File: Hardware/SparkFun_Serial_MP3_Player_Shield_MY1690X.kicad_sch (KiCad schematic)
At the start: 34 parts, among them J1 3.5mm TRRS, J3 Conn_01x03, J4 USB_C_Receptacle, J6 microSD, Q1 BSS138, SW1 SMD_5.2x5.2mm_h2.5mm, U2 MY1690X

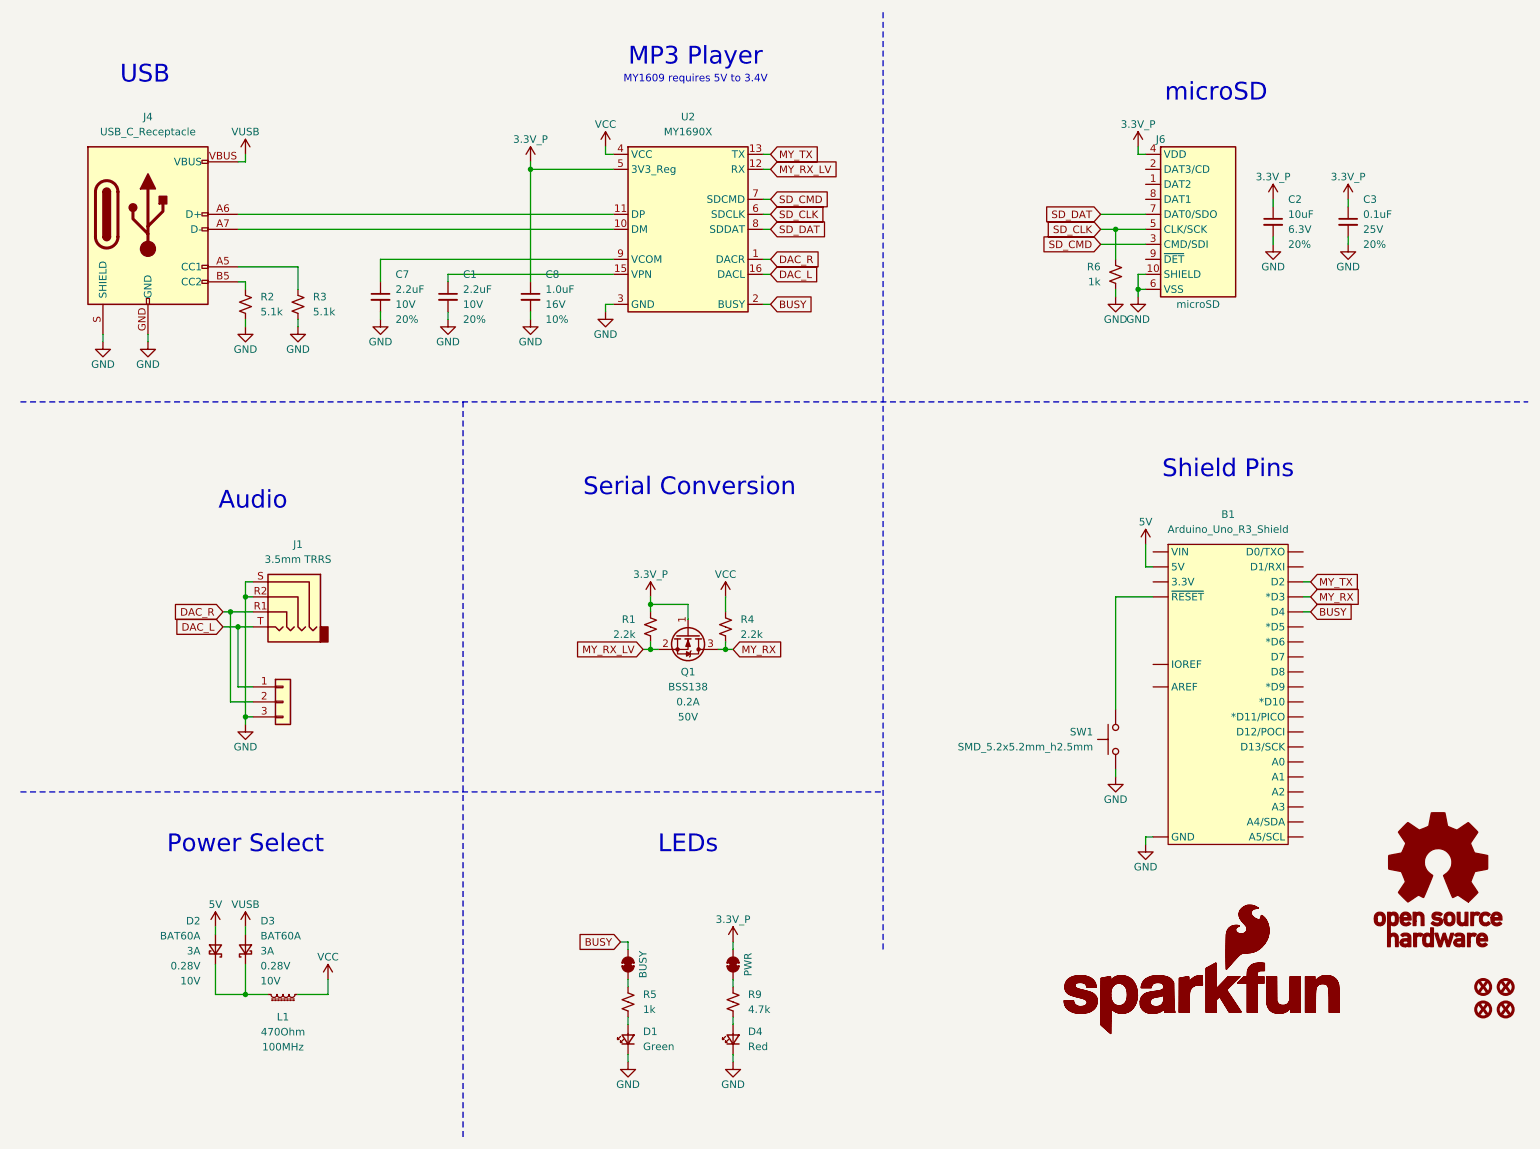
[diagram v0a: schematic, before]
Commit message: Add Busy LED, inline caps to TRRS, card detect, and power filtering.
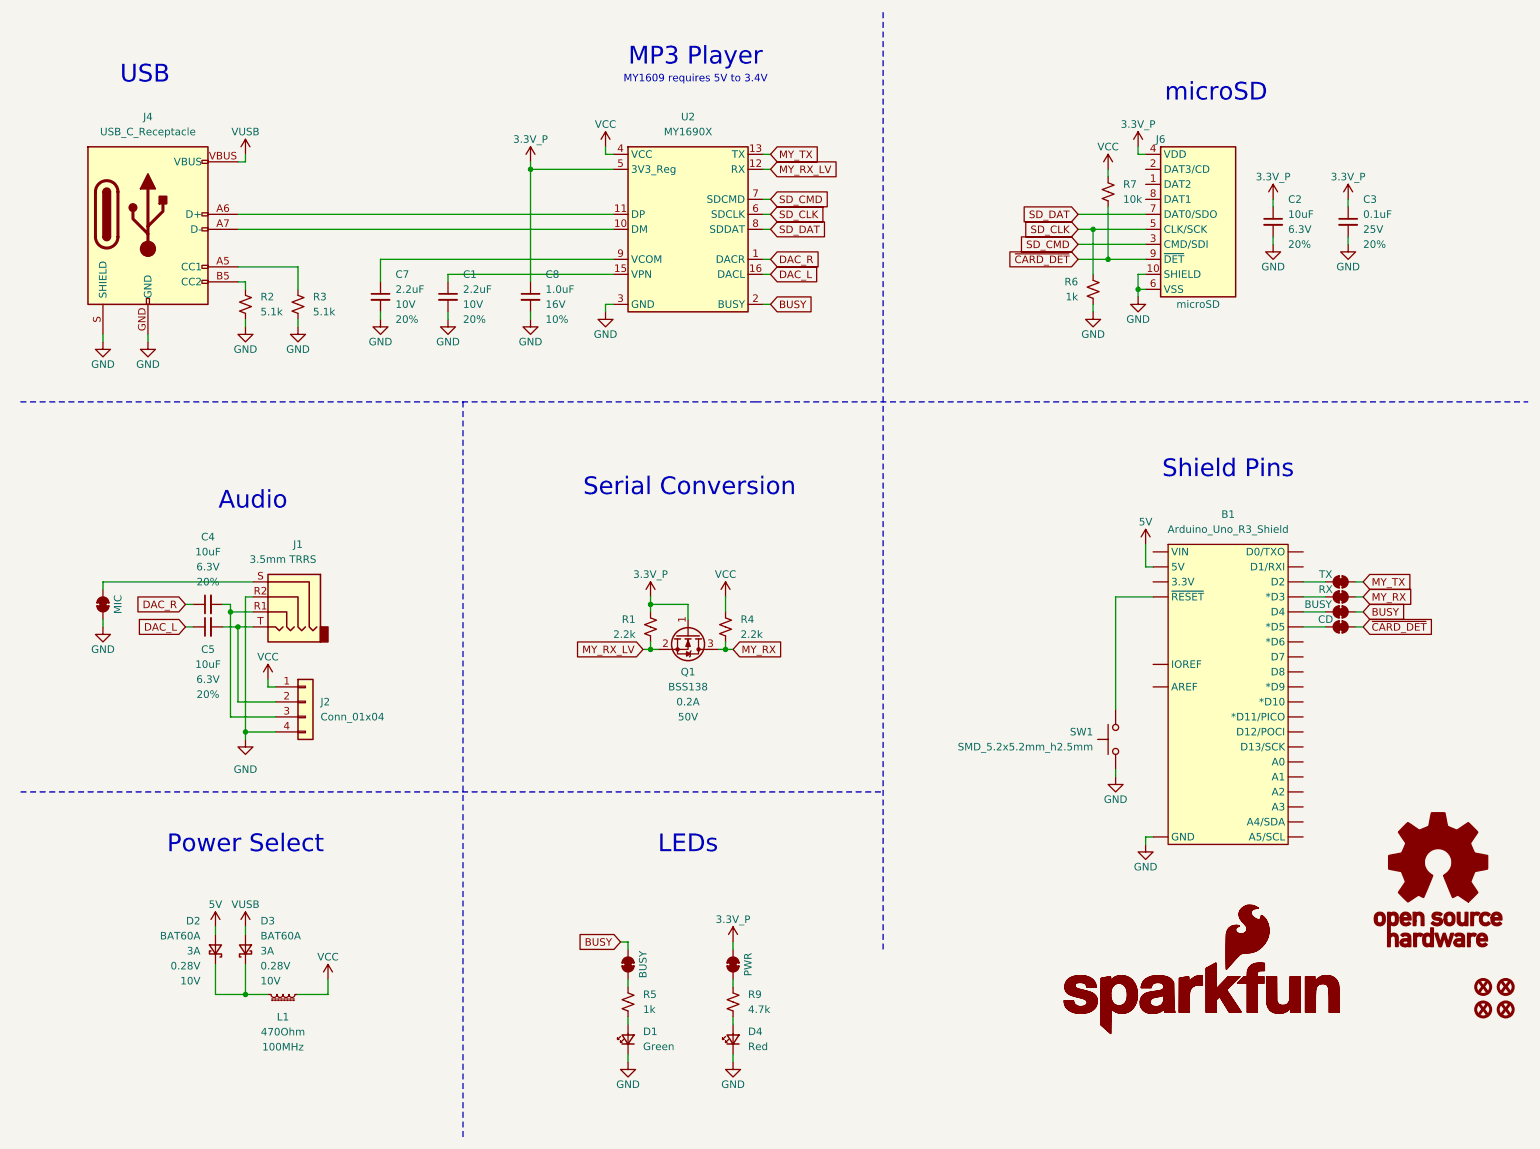
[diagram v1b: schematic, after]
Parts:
- removed J3: Conn_01x03, SparkFun-Connector:1x03, symbol SparkFun-Connector:Conn_01x03
- added C4, C5: 10uF, SparkFun-Capacitor:C_0603_1608Metric, symbol SparkFun-Capacitor:10uF_0603_6.3V_20%
- added J2: Conn_01x04, SparkFun-Connector:1x04, symbol SparkFun-Connector:Conn_01x04
- added JP3: CD, SparkFun-Jumper:Jumper_2_PTH_SMD_Combo-NC, symbol SparkFun-Jumper:Jumper_Measure
- added JP4: BUSY, SparkFun-Jumper:Jumper_2_PTH_SMD_Combo-NC, symbol SparkFun-Jumper:Jumper_Measure
- added JP5: RX, SparkFun-Jumper:Jumper_2_PTH_SMD_Combo-NC, symbol SparkFun-Jumper:Jumper_Measure
- added JP6: TX, SparkFun-Jumper:Jumper_2_PTH_SMD_Combo-NC, symbol SparkFun-Jumper:Jumper_Measure
- added JP7: MIC, SparkFun-Jumper:Jumper_2_NC_Trace, symbol SparkFun-Jumper:SolderJumper_2_Bridged
- added R7: 10k, SparkFun-Resistor:R_0603_1608Metric, symbol SparkFun-Resistor:10k_0603
- J1: symbol SparkFun-Connector:Audio Jack TRRS 3.5mm SMD -> SparkFun-Connector:Audio_Jack_TRRS_3.5mm_SMD; PROD_ID (none) -> CONN-10676
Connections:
- net BUSY: now also JP4.2 (B); no longer B1.D4
- net DAC_L: now also C5.1; no longer J1.T
- net DAC_R: now also C4.1; no longer J1.R1
- net GND: now also J2.4 (Pin_4), JP7.1 (A); no longer J1.S
- net MY_RX: now also JP5.2 (B); no longer B1.D3 (*D3)
- net MY_TX: now also JP6.2 (B); no longer B1.D2
- net VCC: now also J2.1 (Pin_1), R7.2
- net ~{CARD_DET}: now reaches J6.9 (~{DET})
- net ~{CARD_DET}: now also JP3.2 (B), R7.1
- net at B1.D5 (*D5): now also JP3.1 (A)
- new net: C5.2, J1.T, J2.2 (Pin_2)
- new net: C4.2, J1.R1, J2.3 (Pin_3)
- new net: J1.S, JP7.2 (B)
- new net: B1.D3 (*D3), JP5.1 (A)
- new net: B1.D2, JP6.1 (A)
- new net: B1.D4, JP4.1 (A)
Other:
- moved on the sheet: R6

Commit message: Fix PROD ID on TRRS
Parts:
- J1: PROD-ID CONN-10676 -> (none)
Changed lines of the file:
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@@
-			)
-		)
-		(property "PROD-ID" "CONN-10676"
-			(at 57.15 128.27 0)
-			(effects
-				(font
-					(size 1.27 1.27)
-				)
-				(hide yes)
 			)
 		)

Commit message: Post review updates.
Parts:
- removed R6: 1k, SparkFun-Resistor:R_0603_1608Metric, symbol SparkFun-Resistor:1k_0603
- added D5: DT1042-04SO, SparkFun-Semiconductor-Standard:SOT23-6, symbol SparkFun-DiscreteSemi:D_TVS_ESD_USB
- added F1: 6V/0.5A/1A, SparkFun-Fuse:0805, symbol SparkFun-Fuse:Fuse 6V/0.5A/1A
- added J3: Qwiic_RA, SparkFun-Connector:JST_SMD_1.0mm-4_Black, symbol SparkFun-Connector:Qwiic_Right_Angle
- added J5: ISP, SparkFun-Connector:2x03_NoSilk, symbol SparkFun-Connector:AVR_ISP_PTH
- C4, C5: value 10uF -> 47uF; footprint SparkFun-Capacitor:C_0603_1608Metric -> SparkFun-Capacitor:C_0805_2012Metric; symbol SparkFun-Capacitor:10uF_0603_6.3V_20% -> SparkFun-Capacitor:47uF_0805_6.3V_20%; PROD_ID CAP-11015 -> CAP-13854
- JP7: value MIC -> SLV
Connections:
- net GND: now also J2.1 (Pin_1), D5.2 (GND), J3.1 (Pin_1); no longer J2.4 (Pin_4)
- net MY_RX: now also JP6.2 (B); no longer JP5.2 (B)
- net MY_TX: now also JP5.2 (B); no longer JP6.2 (B)
- net VCC: now also J2.4 (Pin_4); no longer J2.1 (Pin_1)
- net VUSB: now also F1.1; no longer J4.VBUS
- net D+: now reaches J4.A6 (D+), J4.B6 (D+), U2.11 (DP)
- net D+: now also D5.6 (I/O4)
- net D-: now reaches J4.A7 (D-), J4.B7 (D-), U2.10 (DM)
- net D-: now also D5.3 (I/O2)
- net at JP5.1 (A): now also B1.D8; no longer B1.D3 (*D3)
- net 3.3V: now reaches B1.3.3V
- net 3.3V: now also J3.2 (Pin_2)
- net SDA: now reaches B1.A4/SDA
- net SDA: now also J3.3 (Pin_3)
- net SCL: now reaches B1.A5/SCL
- net SCL: now also J3.4 (Pin_4)
- net at JP6.1 (A): now also B1.D9 (*D9); no longer B1.D2
- new net: F1.2, J4.VBUS
- no-connect marks 0 -> 28
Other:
- note added: "Cut jumpers to disconnect LEDs"
- note added: "Cut jumpers to move pins"
- note added: "MY1609 requires 3.4 to 5V"
- note added: "Qwiic"
- note added: "SLV can be cut for certain headphones that include a mic"
- note added: "SPI pass through for shield compatibility"
- note removed: "MY1609 requires 5V to 3.4V"
- moved on the sheet: C1, C2, C3, C7, C8, D1, D2, D3, D4, J4, J6, L1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

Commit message: Change Playing resistor to 330
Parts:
- R5: value 1k -> 330; symbol SparkFun-Resistor:1k_0603 -> SparkFun-Resistor:330_0603; PROD_ID RES-07856 -> RES-00818
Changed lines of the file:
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@@
 	)
 	(symbol
-		(lib_id "SparkFun-Resistor:1k_0603")
+		(lib_id "SparkFun-Resistor:330_0603")
 		(at 76.2 179.07 90)
 		(unit 1)
@@
 			)
 		)
-		(property "Value" "1k"
+		(property "Value" "330"
 			(at 78.74 180.3399 90)
 			(effects
@@
 		)
 		(property "Datasheet" "https://www.vishay.com/docs/20035/dcrcwe3.pdf"
-			(at 85.09 180.34 0)
+			(at 85.09 179.07 0)
 			(effects
 				(font
@@
 			)
 		)
-		(property "PROD_ID" "RES-07856"
+		(property "PROD_ID" "RES-00818"
 			(at 83.058 179.07 0)
 			(effects
